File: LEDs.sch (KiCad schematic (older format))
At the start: 120 parts, among them Q1 MOSFET_N, Q2 MOSFET_N, Q3 MOSFET_N, Q4 MOSFET_N, Q5 MOSFET_N, U4 SN74AHC367

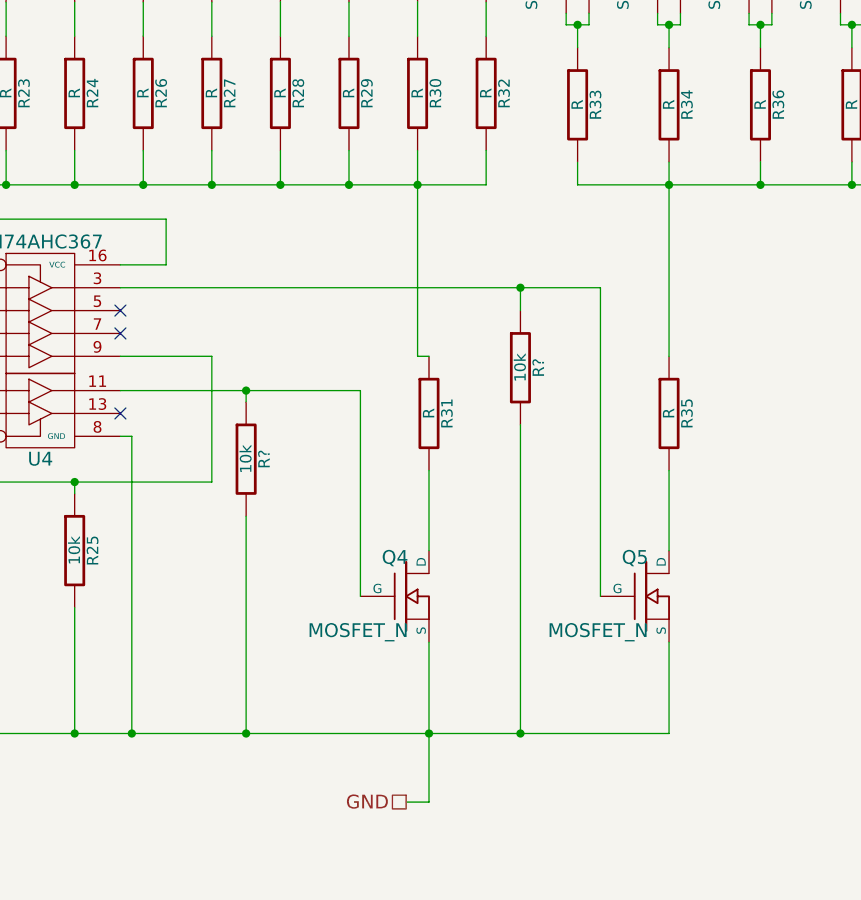
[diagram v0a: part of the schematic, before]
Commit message: 
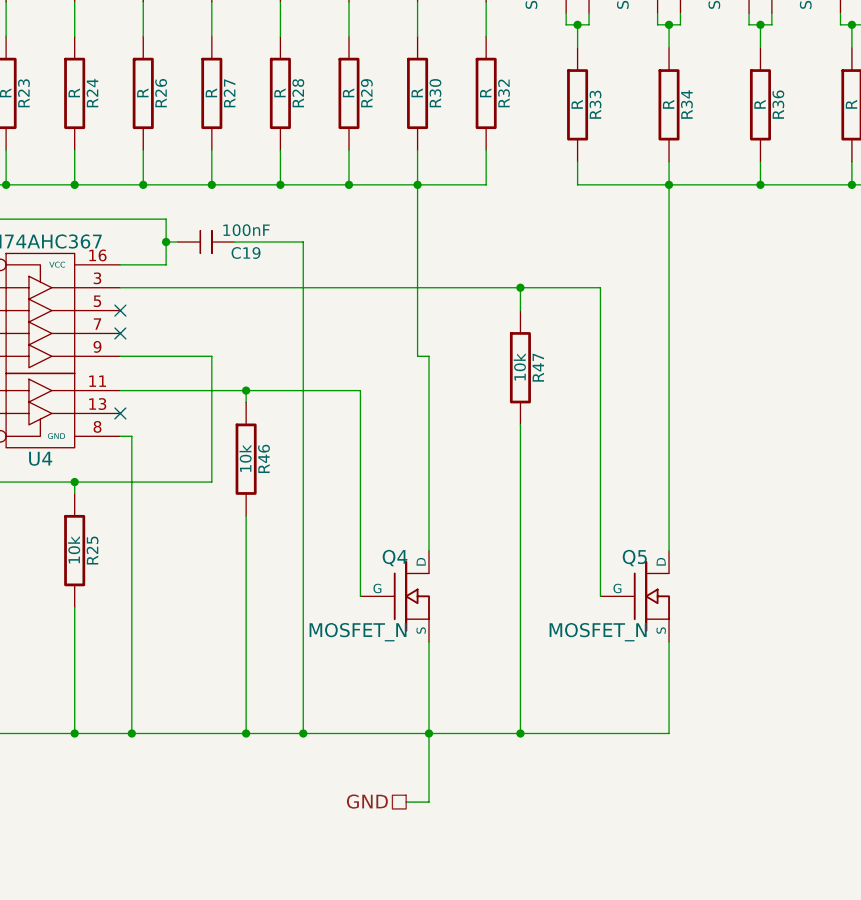
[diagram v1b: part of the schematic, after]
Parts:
- removed R31, R35: R, symbol R
- added C19: 100nF, symbol C
- gave numbers to parts that had none: 2
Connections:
- net 5V: now also C19.2
- net GND: now also C19.1
- net at Q5.D: now also R33.2, R34.2, R36.2, R37.2, R38.2, R39.2
- net at Q4.D: now also R18.2, R19.2, R20.2, R21.2, R22.2, R23.2, R24.2, R26.2, R27.2, R28.2, R29.2, R30.2, R32.2
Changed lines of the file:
@@
-EESchema Schematic File Version 2  date Mi 19 Okt 2011 07:56:14 CEST
+EESchema Schematic File Version 2  date Mi 19 Okt 2011 19:33:39 CEST
 LIBS:rl_con
 LIBS:rl_device
@@
 Comment4 ""
 $EndDescr
+Wire Wire Line
+	9400 4150 9400 5850
+Connection ~ 7800 6650
+Wire Wire Line
+	7800 6650 7800 4500
+Wire Wire Line
+	7800 4500 7500 4500
 Connection ~ 7550 6650
 Wire Wire Line
@@
 Wire Wire Line
 	10200 4250 10200 4150
-Wire Wire Line
-	9400 5000 9400 4150
 Connection ~ 9000 1450
 Wire Wire Line
@@
 	4650 3800 4650 4150
 Wire Wire Line
-	9400 5500 9400 5850
-Wire Wire Line
 	7000 4600 7200 4600
 Wire Wire Line
@@
 	7050 5350 7050 6650
 Connection ~ 7050 6650
-Wire Wire Line
-	8350 5500 8350 5850
 Wire Wire Line
 	4350 3950 2300 3950
@@
 	8750 5300 8750 6650
 Connection ~ 8750 6650
-$Comp
-L R R?
+Wire Wire Line
+	7250 4500 7200 4500
+Connection ~ 7200 4500
+Wire Wire Line
+	8350 5000 8350 5850
+$Comp
+L C C19
+U 1 1 4E9EA371
+P 7350 4500
+F 0 "C19" V 7400 4700 50  0000 C CNN
+F 1 "100nF" V 7300 4700 50  0000 C CNN
+	1    7350 4500
+	0    1    1    0
+$EndComp
+$Comp
+L R R47
 U 1 1 4E9E6656
 P 8750 5050
-F 0 "R?" V 8830 5050 50  0000 C CNN
+F 0 "R47" V 8830 5050 50  0000 C CNN
 F 1 "10k" V 8750 5050 50  0000 C CNN
 	1    8750 5050
@@
 $EndComp
 $Comp
-L R R?
+L R R46
 U 1 1 4E9E6653
 P 7550 5450
-F 0 "R?" V 7630 5450 50  0000 C CNN
+F 0 "R46" V 7630 5450 50  0000 C CNN
 F 1 "10k" V 7550 5450 50  0000 C CNN
 	1    7550 5450
@@
 60mA / 3 LED
 $Comp
-L R R35
-U 1 1 4E9D7D6F
-P 9400 5250
-F 0 "R35" V 9480 5250 50  0000 C CNN
-F 1 "R" V 9400 5250 50  0000 C CNN
-	1    9400 5250
-	1    0    0    -1
-$EndComp
-$Comp
-L R R31
-U 1 1 4E9D7D6B
-P 8350 5250
-F 0 "R31" V 8430 5250 50  0000 C CNN
-F 1 "R" V 8350 5250 50  0000 C CNN
-	1    8350 5250
-	1    0    0    -1
-$EndComp
-$Comp
 L SN74AHCT367 U4

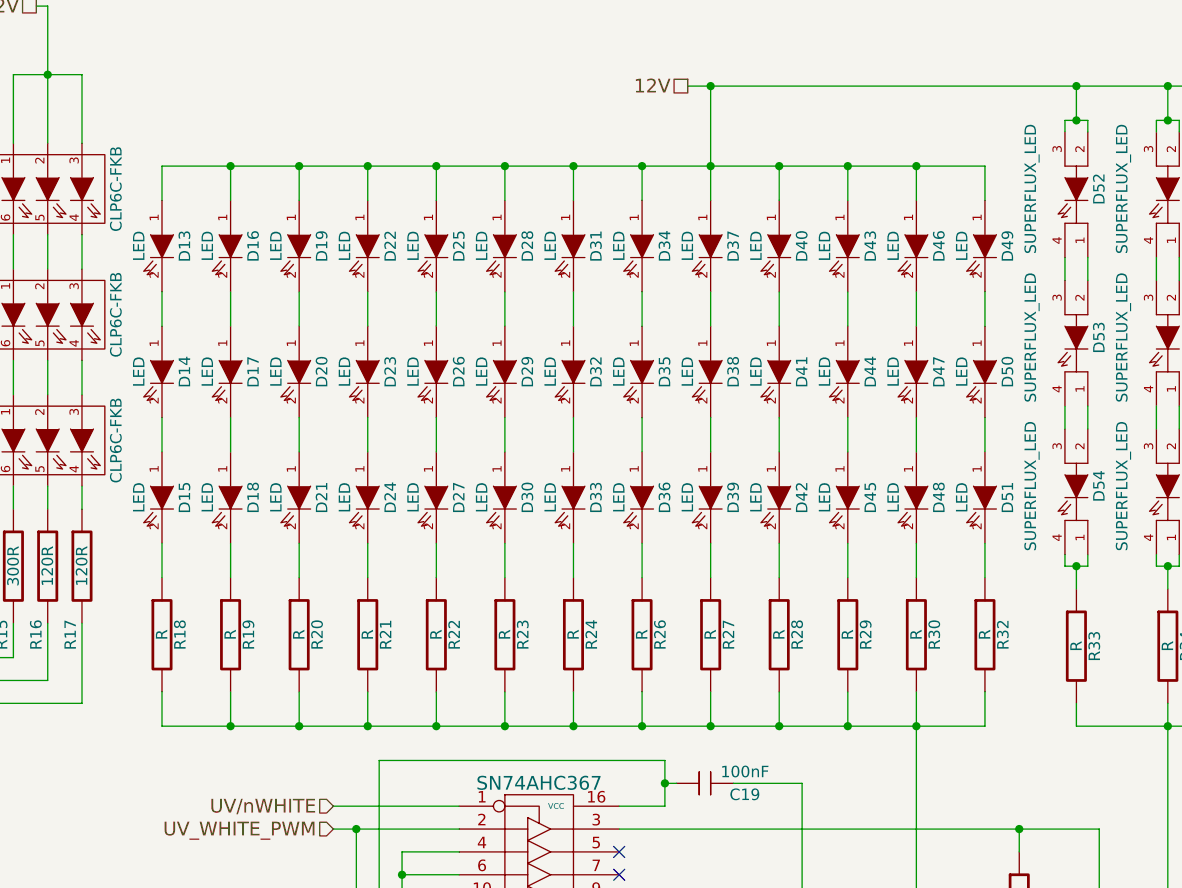
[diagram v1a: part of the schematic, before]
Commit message: 
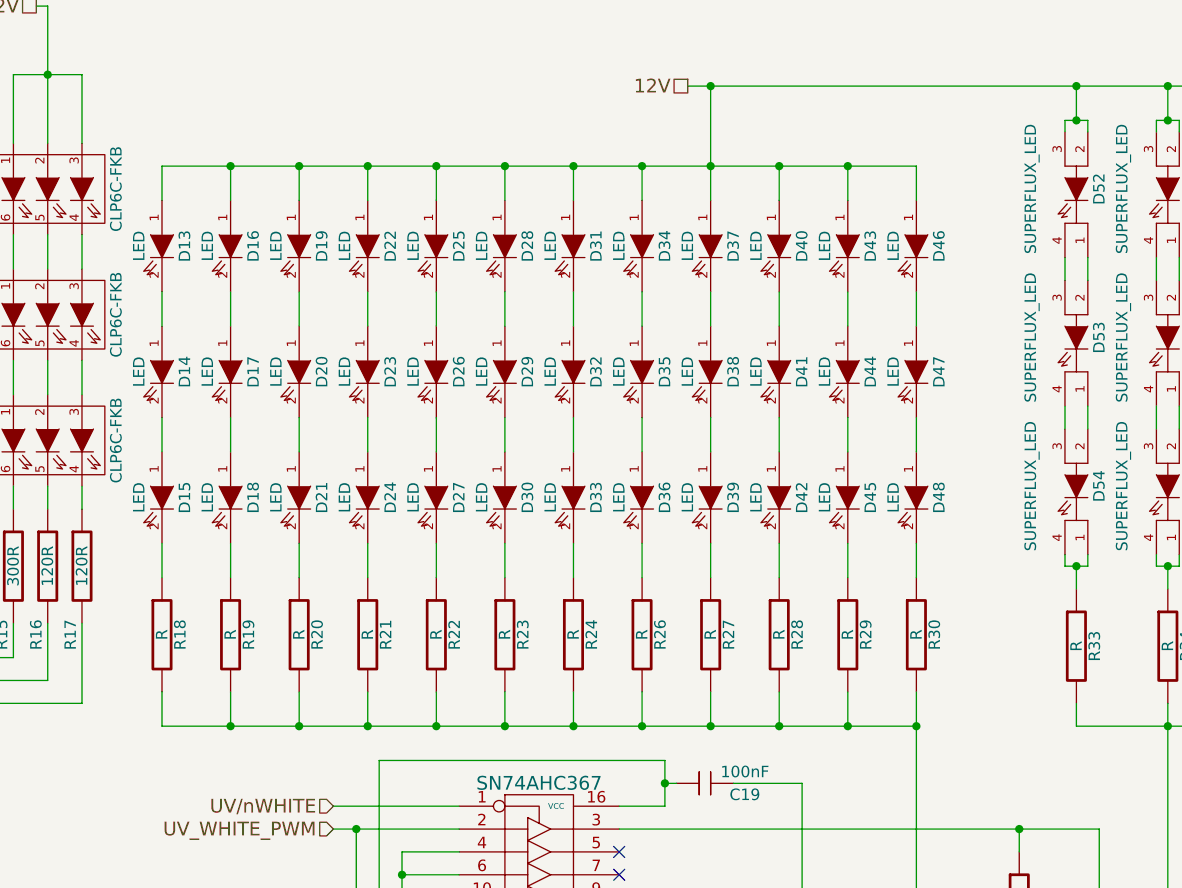
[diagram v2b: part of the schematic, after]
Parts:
- removed D49, D50, D51: LED, symbol LED
- removed R32: R, symbol R
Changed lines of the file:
@@
-EESchema Schematic File Version 2  date Mi 19 Okt 2011 19:33:39 CEST
+EESchema Schematic File Version 2  date So 23 Okt 2011 02:07:59 CEST
 LIBS:rl_con
 LIBS:rl_device
@@
 Sheet 4 5
 Title ""
-Date "19 oct 2011"
+Date "23 oct 2011"
 Rev ""
 Comp ""
@@
 Comment4 ""
 $EndDescr
+Connection ~ 8300 4250
+Wire Wire Line
+	8300 4250 5000 4250
 Wire Wire Line
 	9400 4150 9400 5850
@@
 	7400 4250 7400 4100
 Connection ~ 7400 4250
-Connection ~ 8300 4250
 Connection ~ 7700 4250
 Wire Wire Line
@@
 Wire Wire Line
 	5300 4100 5300 4250
-Connection ~ 8300 1800
 Wire Wire Line
 	8300 1950 8300 1800
@@
 	5600 1800 5600 1950
 Wire Wire Line
-	8600 1950 8600 1800
-Wire Wire Line
-	8600 1800 5000 1800
-Wire Wire Line
-	5000 1800 5000 1950
+	5000 1950 5000 1800
 Wire Wire Line
 	9000 3650 9000 3550
@@
 	8000 3600 8000 3450
 Wire Wire Line
-	8600 3600 8600 3450
-Wire Wire Line
-	8600 3050 8600 2900
-Wire Wire Line
-	8600 2500 8600 2350
-Wire Wire Line
 	8300 2500 8300 2350
 Wire Wire Line
@@
 Connection ~ 7700 1800
 Wire Wire Line
-	5000 4100 5000 4250
-Wire Wire Line
-	5000 4250 8600 4250
-Wire Wire Line
-	8600 4250 8600 4100
+	5000 4250 5000 4100
 Wire Wire Line
 	5600 4250 5600 4100
@@
 Wire Wire Line
 	8350 5000 8350 5850
+Wire Wire Line
+	5000 1800 8300 1800
 $Comp
 L C C19
@@
 $EndComp
 $Comp
-L LED D49
-U 1 1 4E9D873E
-P 8600 2150
-F 0 "D49" H 8600 2250 50  0000 C CNN
-F 1 "LED" H 8600 2050 50  0000 C CNN
-	1    8600 2150
-	0    1    1    0
-$EndComp
-$Comp
-L LED D50
-U 1 1 4E9D873D
-P 8600 2700
-F 0 "D50" H 8600 2800 50  0000 C CNN
-F 1 "LED" H 8600 2600 50  0000 C CNN
-	1    8600 2700
-	0    1    1    0
-$EndComp
-$Comp
-L LED D51
-U 1 1 4E9D873C
-P 8600 3250
-F 0 "D51" H 8600 3350 50  0000 C CNN
-F 1 "LED" H 8600 3150 50  0000 C CNN
-	1    8600 3250
-	0    1    1    0
-$EndComp
-$Comp
-L R R32
-U 1 1 4E9D873B
-P 8600 3850
-F 0 "R32" V 8680 3850 50  0000 C CNN
-F 1 "R" V 8600 3850 50  0000 C CNN
-	1    8600 3850
-	1    0    0    -1
-$EndComp
-$Comp

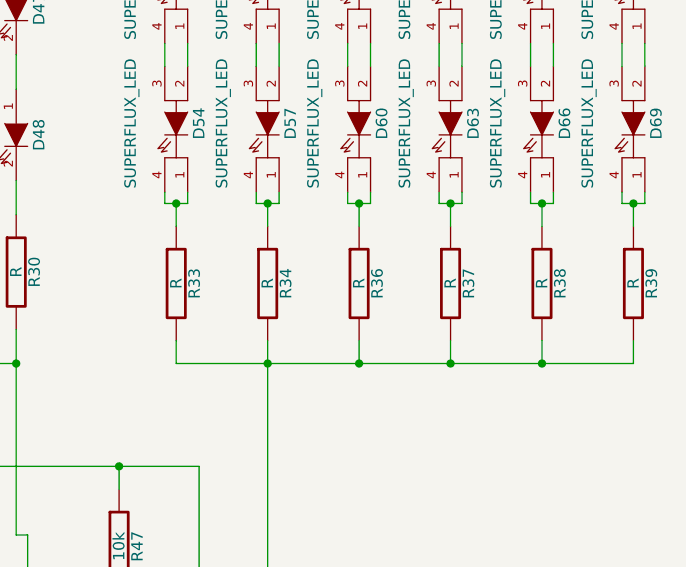
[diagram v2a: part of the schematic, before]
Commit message: 
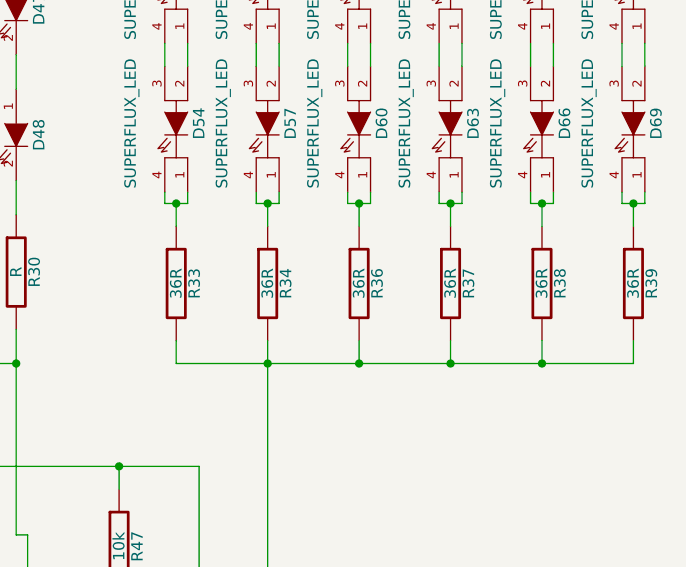
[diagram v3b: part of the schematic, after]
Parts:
- R33, R34, R36, R37, R38, R39: value R -> 36R
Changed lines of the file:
@@
-EESchema Schematic File Version 2  date So 23 Okt 2011 02:07:59 CEST
+EESchema Schematic File Version 2  date Mo 24 Okt 2011 16:23:56 CEST
 LIBS:rl_con
 LIBS:rl_device
@@
 Sheet 4 5
 Title ""
-Date "23 oct 2011"
+Date "24 oct 2011"
 Rev ""
 Comp ""
@@
 P 11000 3900
 F 0 "R39" V 11080 3900 50  0000 C CNN
-F 1 "R" V 11000 3900 50  0000 C CNN
+F 1 "36R" V 11000 3900 50  0000 C CNN
 	1    11000 3900
 	1    0    0    -1
@@
 P 10600 3900
 F 0 "R38" V 10680 3900 50  0000 C CNN
-F 1 "R" V 10600 3900 50  0000 C CNN
+F 1 "36R" V 10600 3900 50  0000 C CNN
 	1    10600 3900
 	1    0    0    -1
@@
 P 10200 3900
 F 0 "R37" V 10280 3900 50  0000 C CNN
-F 1 "R" V 10200 3900 50  0000 C CNN
+F 1 "36R" V 10200 3900 50  0000 C CNN
 	1    10200 3900
 	1    0    0    -1
@@
 P 9800 3900
 F 0 "R36" V 9880 3900 50  0000 C CNN
-F 1 "R" V 9800 3900 50  0000 C CNN
+F 1 "36R" V 9800 3900 50  0000 C CNN
 	1    9800 3900
 	1    0    0    -1
@@
 P 9400 3900
 F 0 "R34" V 9480 3900 50  0000 C CNN
-F 1 "R" V 9400 3900 50  0000 C CNN
+F 1 "36R" V 9400 3900 50  0000 C CNN
 	1    9400 3900
 	1    0    0    -1
@@
 P 9000 3900
 F 0 "R33" V 9080 3900 50  0000 C CNN
-F 1 "R" V 9000 3900 50  0000 C CNN
+F 1 "36R" V 9000 3900 50  0000 C CNN
 	1    9000 3900
 	1    0    0    -1

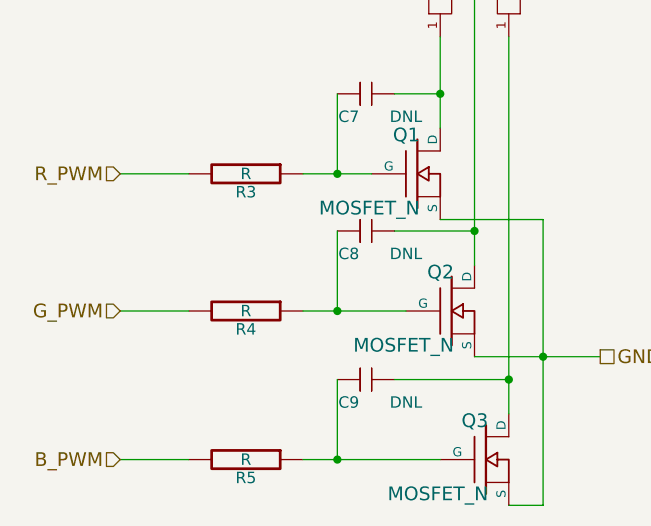
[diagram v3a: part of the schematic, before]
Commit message: 
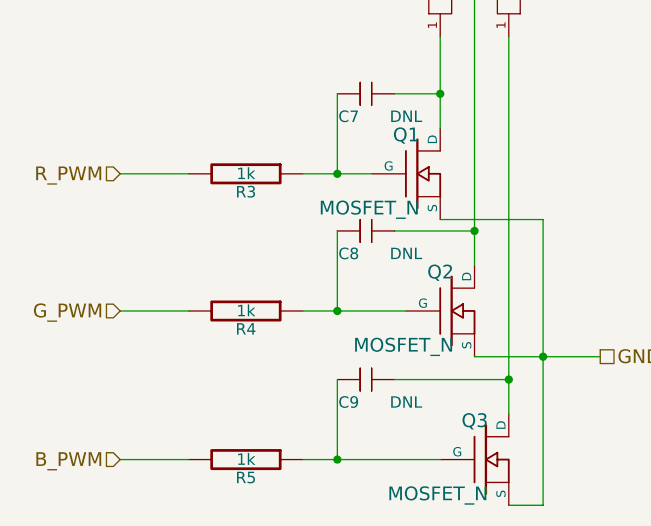
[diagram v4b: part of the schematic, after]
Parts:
- R3, R4, R5: value R -> 1k
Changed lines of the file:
@@
-EESchema Schematic File Version 2  date Mo 24 Okt 2011 16:23:56 CEST
+EESchema Schematic File Version 2  date Do 03 Nov 2011 14:47:05 CET
 LIBS:rl_con
 LIBS:rl_device
@@
 Sheet 4 5
 Title ""
-Date "24 oct 2011"
+Date "3 nov 2011"
 Rev ""
 Comp ""
@@
 P 1600 7450
 F 0 "R5" V 1680 7450 50  0000 C CNN
-F 1 "R" V 1600 7450 50  0000 C CNN
+F 1 "1k" V 1600 7450 50  0000 C CNN
 	1    1600 7450
 	0    1    1    0
@@
 P 1600 6800
 F 0 "R4" V 1680 6800 50  0000 C CNN
-F 1 "R" V 1600 6800 50  0000 C CNN
+F 1 "1k" V 1600 6800 50  0000 C CNN
 	1    1600 6800
 	0    1    1    0
@@
 P 1600 6200
 F 0 "R3" V 1680 6200 50  0000 C CNN
-F 1 "R" V 1600 6200 50  0000 C CNN
+F 1 "1k" V 1600 6200 50  0000 C CNN
 	1    1600 6200
 	0    1    1    0
